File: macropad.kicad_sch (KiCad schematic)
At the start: 65 parts, among them J1 USB_C_Receptacle_USB2.0, J3 Conn_01x03, J6 Conn_01x04_Pin, J7 Conn_01x02_Pin, SW1 SW_Push, SW2 SW_Push, SW3 SW_Push, SW4 SW_Push, SW5 SW_Push, SW6 RotaryEncoder_Switch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

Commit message: Cleanup libraries
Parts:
- LED1, LED2, LED3, LED4, LED5, LED6: symbol marbastlib:SK6812MINI-E -> Marbastlib:SK6812MINI-E
- U3: symbol mcp5323:MIC5323-3.3YD5-TR -> Mcp5323:MIC5323-3.3YD5-TR
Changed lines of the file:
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@@
     )
   )
-  (symbol (lib_id "marbastlib:SK6812MINI-E") (at 228.6 118.11 0) (unit 1)
+  (symbol (lib_id "Marbastlib:SK6812MINI-E") (at 228.6 118.11 0) (unit 1)
     (in_bom yes) (on_board yes) (dnp no)
     (property "Reference" "LED4" (at 234.95 125.73 0)
@@
     )
   )
-  (symbol (lib_id "marbastlib:SK6812MINI-E") (at 193.04 118.11 0) (unit 1)
+  (symbol (lib_id "Marbastlib:SK6812MINI-E") (at 193.04 118.11 0) (unit 1)
     (in_bom yes) (on_board yes) (dnp no)
     (property "Reference" "LED2" (at 199.39 125.73 0)
@@
     )
   )
-  (symbol (lib_id "marbastlib:SK6812MINI-E") (at 175.26 118.11 0) (unit 1)
+  (symbol (lib_id "Marbastlib:SK6812MINI-E") (at 175.26 118.11 0) (unit 1)
     (in_bom yes) (on_board yes) (dnp no)
     (property "Reference" "LED1" (at 181.61 125.73 0)
@@
     )
   )
-  (symbol (lib_id "marbastlib:SK6812MINI-E") (at 246.38 118.11 0) (unit 1)
+  (symbol (lib_id "Marbastlib:SK6812MINI-E") (at 246.38 118.11 0) (unit 1)
     (in_bom yes) (on_board yes) (dnp no)
     (property "Reference" "LED5" (at 252.73 125.73 0)
@@
     )
   )
-  (symbol (lib_id "marbastlib:SK6812MINI-E") (at 264.16 118.11 0) (unit 1)
+  (symbol (lib_id "Marbastlib:SK6812MINI-E") (at 264.16 118.11 0) (unit 1)
     (in_bom yes) (on_board yes) (dnp no)
     (property "Reference" "LED6" (at 270.51 125.73 0)
@@
     )
   )
-  (symbol (lib_id "mcp5323:MIC5323-3.3YD5-TR") (at 35.56 168.91 0) (unit 1)
+  (symbol (lib_id "Mcp5323:MIC5323-3.3YD5-TR") (at 35.56 168.91 0) (unit 1)
     (in_bom yes) (on_board yes) (dnp no) (fields_autoplaced)
     (property "Reference" "U3" (at 49.53 161.29 0)
@@
     )
   )
-  (symbol (lib_id "marbastlib:SK6812MINI-E") (at 210.82 118.11 0) (unit 1)
+  (symbol (lib_id "Marbastlib:SK6812MINI-E") (at 210.82 118.11 0) (unit 1)
     (in_bom yes) (on_board yes) (dnp no)
     (property "Reference" "LED3" (at 217.17 125.73 0)

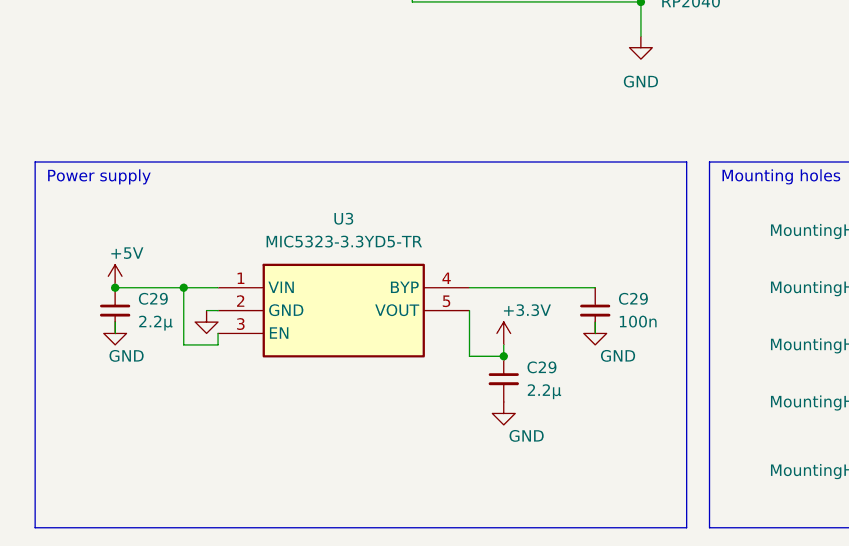
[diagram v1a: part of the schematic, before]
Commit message: Switch LDO for a cheaper part.
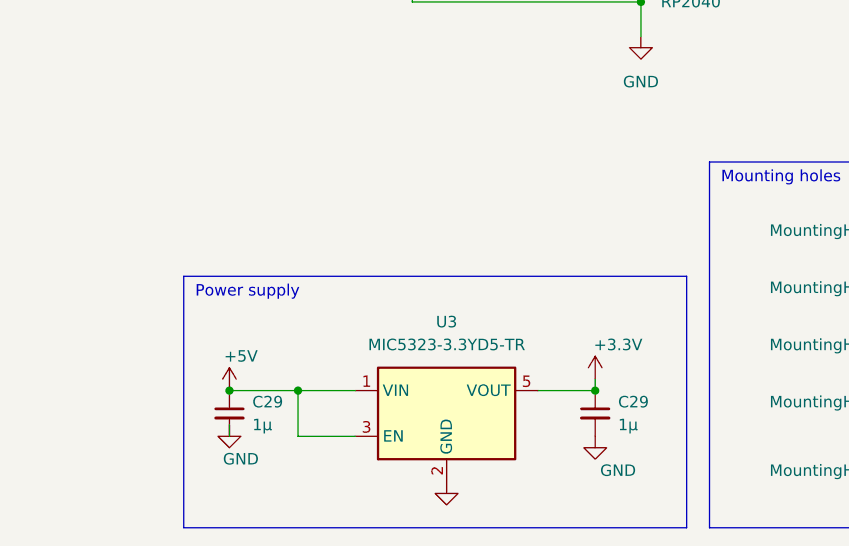
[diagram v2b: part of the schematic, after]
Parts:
- removed C29: 100n, Capacitor_SMD:C_0402_1005Metric, symbol Device:C_Small
- C29: value 2.2µ -> 1µ
- SW1: LCSC (none) -> C5333465
- U3: footprint Trackpad:SOT95P280X100-5N -> Package_TO_SOT_SMD:SOT-23-5; symbol Mcp5323:MIC5323-3.3YD5-TR -> Regulator_Linear:MIC5504-3.3YM5; LCSC C512211 -> C88419
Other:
- moved on the sheet: C29

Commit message: Move USB port closer to the edge, Additional silkscreen, Add reset header, shrink LDO caps, swap QSPI flash.
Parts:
- added J9: Conn_01x02_Pin, Connector_PinHeader_2.54mm:PinHeader_1x02_P2.54mm_Vertical, symbol Connector:Conn_01x02_Pin
- C29: footprint Capacitor_SMD:C_0603_1608Metric -> Capacitor_SMD:C_0402_1005Metric
- SW1: LCSC C5333465 -> (none)
- U2: value GD25Q80CEIGR -> W25Q16JVUXIQ
- U3: LCSC C88419 -> C512211
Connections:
- net D+: now also J1.A6 (D+), J1.B6 (D+), U7.1 (I/O1)
- net D-: now also J1.A7 (D-), J1.B7 (D-), U7.6 (I/O1)
- net GND: now also J9.2 (Pin_2)
- net RUN: now reaches U1.26 (RUN)
- net RUN: now also J9.1 (Pin_1)
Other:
- note added: "Reset Header"
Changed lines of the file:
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@@
   (junction (at 105.41 22.86) (diameter 0) (color 0 0 0 0)
   )
-  (junction (at 218.44 63.5) (diameter 0) (color 0 0 0 0)
-  )
   (junction (at 156.21 31.75) (diameter 0) (color 0 0 0 0)
   )
@@
   (junction (at 77.47 20.32) (diameter 0) (color 0 0 0 0)
   )
+  (junction (at 218.44 63.5) (diameter 0) (color 0 0 0 0)
+  )
   (junction (at 246.38 44.45) (diameter 0) (color 0 0 0 0)
   )
@@
   (junction (at 77.47 180.34) (diameter 0) (color 0 0 0 0)
   )
-  (junction (at 218.44 58.42) (diameter 0) (color 0 0 0 0)
-  )
   (junction (at 82.55 137.16) (diameter 0) (color 0 0 0 0)
   )
@@
   (junction (at 58.42 29.21) (diameter 0) (color 0 0 0 0)
   )
+  (junction (at 218.44 58.42) (diameter 0) (color 0 0 0 0)
+  )
   (junction (at 120.65 62.23) (diameter 0) (color 0 0 0 0)
   )
@@
     (stroke (width 0) (type default))
   )
-  (wire (pts (xy 218.44 63.5) (xy 247.65 63.5))
-    (stroke (width 0) (type default))
-  )
   (wire (pts (xy 175.26 100.33) (xy 179.07 100.33))
     (stroke (width 0) (type default))
@@
     (stroke (width 0) (type default))
   )
-  (wire (pts (xy 218.44 62.23) (xy 218.44 63.5))
+  (wire (pts (xy 222.25 63.5) (xy 218.44 63.5))
     (stroke (width 0) (type default))
   )
@@
     (stroke (width 0) (type default))
   )
-  (wire (pts (xy 218.44 63.5) (xy 218.44 64.77))
+  (wire (pts (xy 218.44 62.23) (xy 218.44 63.5))
     (stroke (width 0) (type default))
   )
@@
     (stroke (width 0) (type default))
   )
+  (wire (pts (xy 218.44 58.42) (xy 218.44 59.69))
+    (stroke (width 0) (type default))
+  )
   (wire (pts (xy 254 118.11) (xy 256.54 118.11))
     (stroke (width 0) (type default))
@@
     (stroke (width 0) (type default))
   )
+  (wire (pts (xy 222.25 58.42) (xy 218.44 58.42))
+    (stroke (width 0) (type default))
+  )
   (wire (pts (xy 210.82 100.33) (xy 210.82 110.49))
     (stroke (width 0) (type default))
@@
     (stroke (width 0) (type default))
   )
+  (wire (pts (xy 243.84 58.42) (xy 247.65 58.42))
+    (stroke (width 0) (type default))
+  )
   (wire (pts (xy 271.78 58.42) (xy 267.97 58.42))
     (stroke (width 0) (type default))
@@
     (stroke (width 0) (type default))
   )
+  (wire (pts (xy 243.84 63.5) (xy 247.65 63.5))
+    (stroke (width 0) (type default))
+  )
   (wire (pts (xy 124.46 64.77) (xy 130.81 64.77))
     (stroke (width 0) (type default))
@@
     (stroke (width 0) (type default))
   )
-  (wire (pts (xy 218.44 57.15) (xy 218.44 58.42))
-    (stroke (width 0) (type default))
-  )
   (wire (pts (xy 77.47 39.37) (xy 77.47 44.45))
     (stroke (width 0) (type default))
@@
     (stroke (width 0) (type default))
   )
+  (wire (pts (xy 80.01 156.21) (xy 76.2 156.21))
+    (stroke (width 0) (type default))
+  )
   (wire (pts (xy 58.42 29.21) (xy 68.58 29.21))
     (stroke (width 0) (type default))
@@
     (stroke (width 0) (type default))
   )
+  (wire (pts (xy 218.44 63.5) (xy 218.44 64.77))
+    (stroke (width 0) (type default))
+  )
   (wire (pts (xy 228.6 100.33) (xy 232.41 100.33))
     (stroke (width 0) (type default))
@@
     (stroke (width 0) (type default))
   )
-  (wire (pts (xy 218.44 58.42) (xy 247.65 58.42))
-    (stroke (width 0) (type default))
-  )
   (wire (pts (xy 120.65 62.23) (xy 130.81 62.23))
     (stroke (width 0) (type default))
@@
     (stroke (width 0) (type default))
   )
-  (wire (pts (xy 218.44 58.42) (xy 218.44 59.69))
+  (wire (pts (xy 218.44 57.15) (xy 218.44 58.42))
     (stroke (width 0) (type default))
   )
@@
     (fill (type none))
   )
+  (rectangle (start 57.15 149.86) (end 87.63 165.1)
+    (stroke (width 0) (type default))
+    (fill (type none))
+  )
   (rectangle (start 189.23 33.02) (end 280.67 88.9)
     (stroke (width 0) (type default))
@@
     (effects (font (size 1.27 1.27)) (justify left bottom))
   )
+  (text "Reset Header" (at 58.42 152.4 0)
+    (effects (font (size 1.27 1.27)) (justify left bottom))
+  )
   (text "5V LED\nData" (at 158.75 123.19 0)
     (effects (font (size 1.27 1.27)) (justify left bottom))
@@
     (effects (font (size 1.27 1.27)) (justify right bottom))
   )
+  (label "RUN" (at 80.01 156.21 0) (fields_autoplaced)
+    (effects (font (size 1.27 1.27)) (justify left bottom))
+  )
   (label "ENC2_A" (at 107.95 97.79 0) (fields_autoplaced)
     (effects (font (size 1.27 1.27)) (justify left bottom))
@@
     (effects (font (size 1.27 1.27)) (justify right bottom))
   )
+  (label "RUN" (at 57.15 52.07 180) (fields_autoplaced)
+    (effects (font (size 1.27 1.27)) (justify right bottom))
+  )
   (label "SW1" (at 151.13 147.32 0) (fields_autoplaced)
     (effects (font (size 1.27 1.27)) (justify left bottom))
@@
     (effects (font (size 1.27 1.27)) (justify left bottom))
   )
+  (label "D-" (at 243.84 58.42 180) (fields_autoplaced)
+    (effects (font (size 1.27 1.27)) (justify right bottom))
+  )
+  (label "D-" (at 222.25 58.42 0) (fields_autoplaced)
+    (effects (font (size 1.27 1.27)) (justify left bottom))
+  )
   (label "SW7" (at 234.95 152.4 180) (fields_autoplaced)
     (effects (font (size 1.27 1.27)) (justify right bottom))
@@
     (effects (font (size 1.27 1.27)) (justify right bottom))
   )
+  (label "D+" (at 222.25 63.5 0) (fields_autoplaced)
+    (effects (font (size 1.27 1.27)) (justify left bottom))
+  )
+  (label "D+" (at 243.84 63.5 180) (fields_autoplaced)
+    (effects (font (size 1.27 1.27)) (justify right bottom))
+  )
   (label "D-" (at 271.78 58.42 0) (fields_autoplaced)
     (effects (font (size 1.27 1.27)) (justify left bottom))
@@
       (effects (font (size 1.27 1.27)) (justify left))
     )
-    (property "Footprint" "Capacitor_SMD:C_0603_1608Metric" (at 77.47 182.88 0)
+    (property "Footprint" "Capacitor_SMD:C_0402_1005Metric" (at 77.47 182.88 0)
       (effects (font (size 1.27 1.27)) hide)
     )
@@
     )
   )
+  (symbol (lib_id "power:GND") (at 76.2 158.75 90) (unit 1)
+    (in_bom yes) (on_board yes) (dnp no) (fields_autoplaced)
+    (property "Reference" "#PWR01" (at 82.55 158.75 0)
+      (effects (font (size 1.27 1.27)) hide)
+    )
+    (property "Value" "GND" (at 80.01 158.75 90)
+      (effects (font (size 1.27 1.27)) (justify right))
+    )
+    (property "Footprint" "" (at 76.2 158.75 0)
+      (effects (font (size 1.27 1.27)) hide)
+    )
+    (property "Datasheet" "" (at 76.2 158.75 0)
+      (effects (font (size 1.27 1.27)) hide)
+    )
+    (pin "1")
+    (instances
+      (project "trackpad"
+        (path "/3796446b-0052-4d89-b512-07a2e9135d0d"
+          (reference "#PWR01") (unit 1)
+        )
+        (path "/3796446b-0052-4d89-b512-07a2e9135d0d/efc97fde-28db-4fd6-89b1-84dafa779b4e"
+          (reference "#PWR051") (unit 1)
+        )
+      )
+    )
+  )
   (symbol (lib_id "power:GND") (at 199.39 83.82 0) (unit 1)
     (in_bom yes) (on_board yes) (dnp no)
@@
       (effects (font (size 1.27 1.27)) (justify left))
     )
-    (property "Value" "GD25Q80CEIGR" (at 40.64 90.17 0)
+    (property "Value" "W25Q16JVUXIQ" (at 40.64 90.17 0)
       (effects (font (size 1.27 1.27)) (justify left))
     )
@@
       (effects (font (size 1.27 1.27)) (justify left))
     )
-    (property "Footprint" "Capacitor_SMD:C_0603_1608Metric" (at 36.83 182.88 0)
+    (property "Footprint" "Capacitor_SMD:C_0402_1005Metric" (at 36.83 182.88 0)
       (effects (font (size 1.27 1.27)) hide)
     )
@@
     )
   )
+  (symbol (lib_id "Connector:Conn_01x02_Pin") (at 71.12 156.21 0) (unit 1)
+    (in_bom yes) (on_board yes) (dnp no)
+    (property "Reference" "J9" (at 77.47 153.67 0)
+      (effects (font (size 1.27 1.27)))
+    )
+    (property "Value" "Conn_01x02_Pin" (at 68.58 161.29 0)
+      (effects (font (size 1.27 1.27)))
+    )
+    (property "Footprint" "Connector_PinHeader_2.54mm:PinHeader_1x02_P2.54mm_Vertical" (at 71.12 156.21 0)
+      (effects (font (size 1.27 1.27)) hide)
+    )
+    (property "Datasheet" "~" (at 71.12 156.21 0)
+      (effects (font (size 1.27 1.27)) hide)
+    )
+    (pin "1")
+    (pin "2")
+    (instances
+      (project "trackpad"
+        (path "/3796446b-0052-4d89-b512-07a2e9135d0d/efc97fde-28db-4fd6-89b1-84dafa779b4e"
+          (reference "J9") (unit 1)
+        )
+      )
+    )
+  )
   (symbol (lib_id "Device:D_Schottky") (at 242.57 44.45 0) (mirror y) (unit 1)
     (in_bom yes) (on_board yes) (dnp no)
@@
       (effects (font (size 1.27 1.27)) (justify left top) hide)
     )
-    (property "LCSC" "C88419" (at 74.93 175.26 0)
+    (property "LCSC" "C512211" (at 74.93 175.26 0)
       (effects (font (size 1.27 1.27)) hide)
     )
@@
       (effects (font (size 1.27 1.27)) hide)
     )
-    (property "LCSC" "C5333465" (at 38.1 44.45 0)
-      (effects (font (size 1.27 1.27)) hide)
-    )

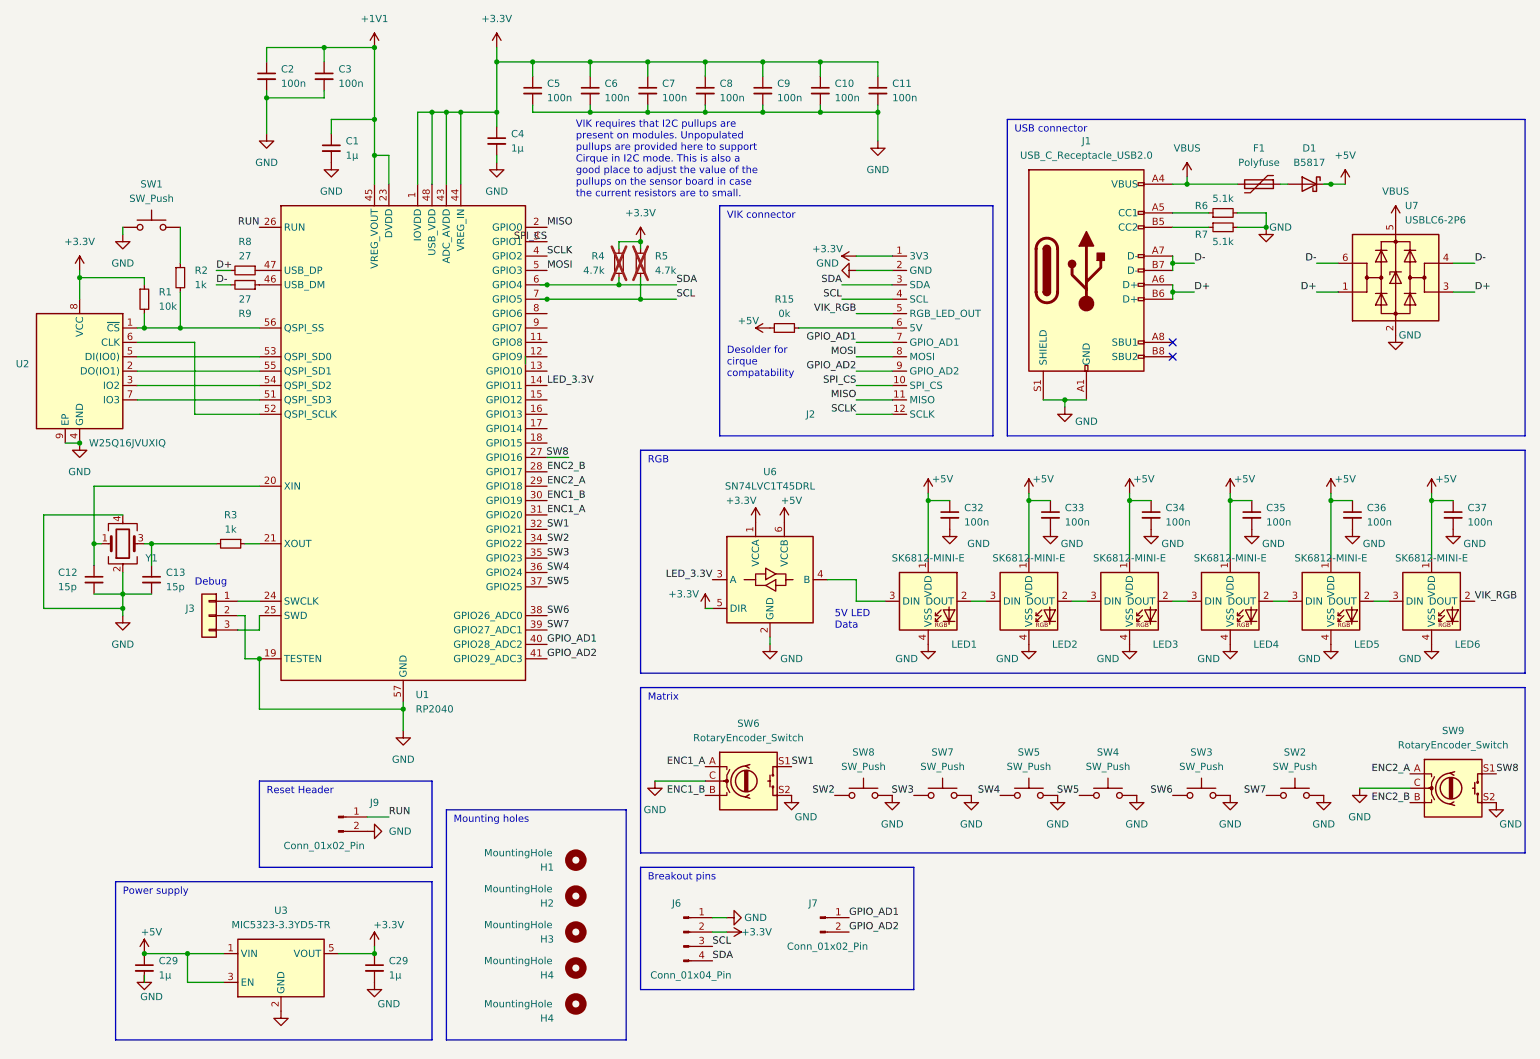
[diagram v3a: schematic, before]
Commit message: Re-route to avoid crossing the USB data lines. Reduced keys to 5 to avoid having to route a long trace around the crystal, swaped key footprint from choc hotswap to mx/choc combined soldered.
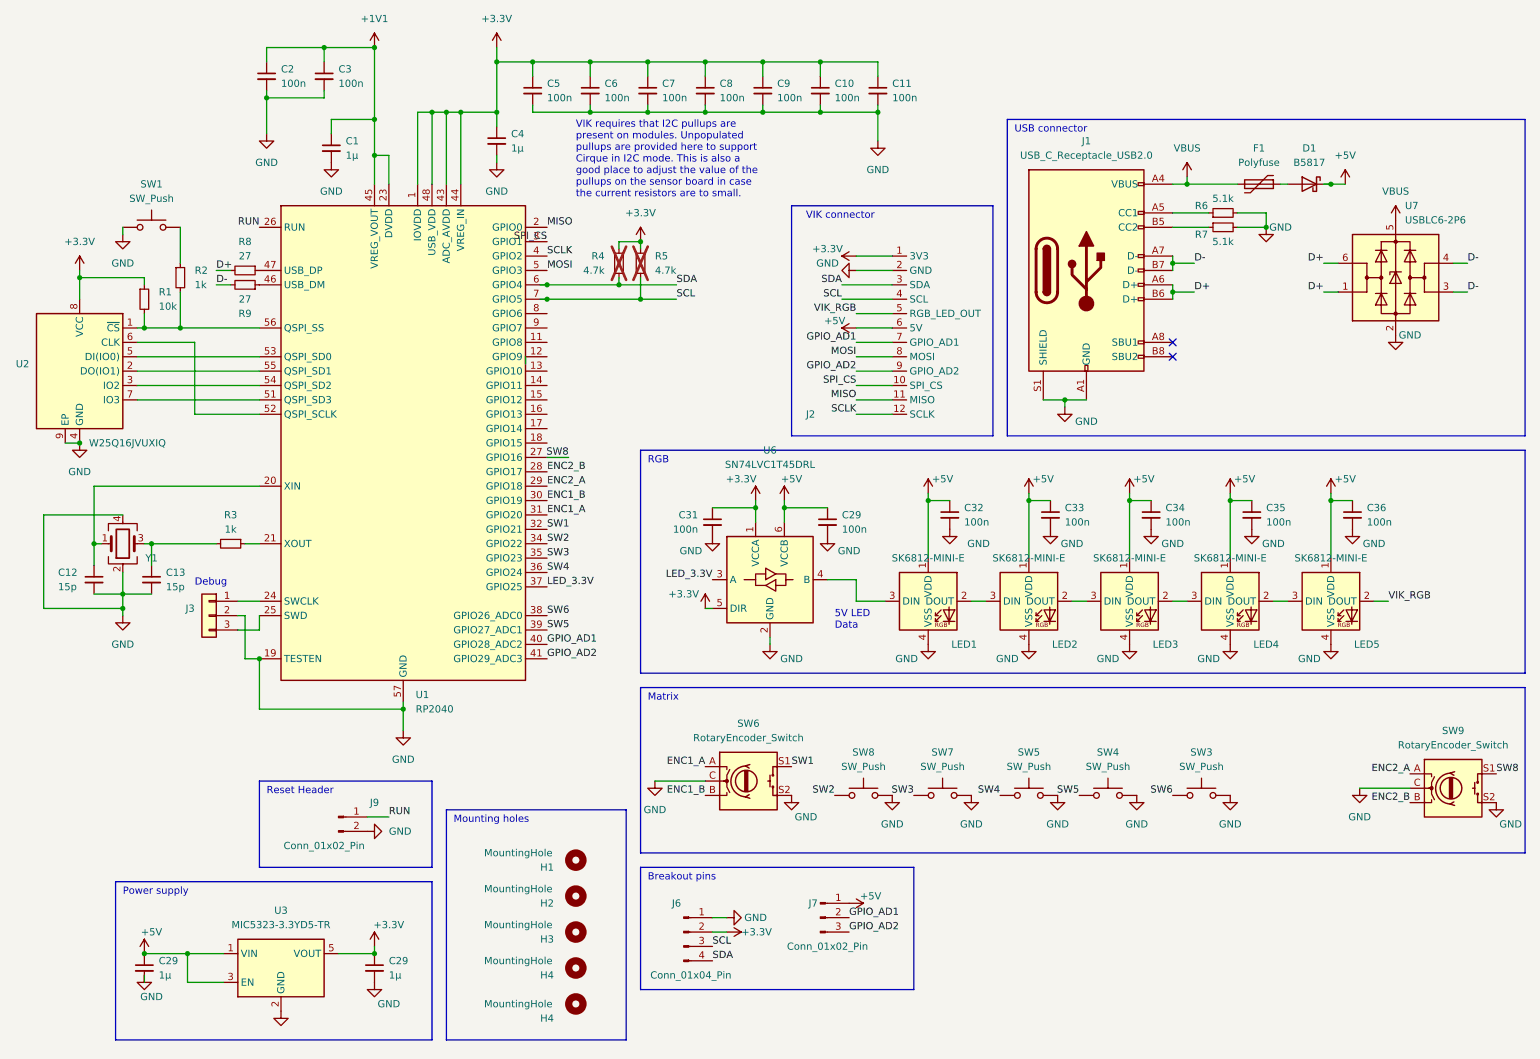
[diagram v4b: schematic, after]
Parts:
- removed C37: 100n, Capacitor_SMD:C_0402_1005Metric, symbol Device:C_Small
- removed LED6: SK6812-MINI-E, PCM_marbastlib-various:LED_6028R, symbol Marbastlib:SK6812MINI-E
- removed R15: 0k, Resistor_SMD:R_0402_1005Metric_Pad0.72x0.64mm_HandSolder, symbol Device:R_Small
- removed SW2: SW_Push, PCM_marbastlib-choc:SW_choc_v1_HS_1u, symbol Switch:SW_Push
- added C29, C31: 100n, Capacitor_SMD:C_0402_1005Metric, symbol Device:C_Small
- H2: footprint MountingHole:MountingHole_3.2mm_M3 -> MountingHole:MountingHole_2.2mm_M2
- J7: footprint Connector_PinHeader_2.54mm:PinHeader_1x02_P2.54mm_Vertical -> Connector_PinHeader_2.54mm:PinHeader_1x03_P2.54mm_Vertical; symbol Connector:Conn_01x02_Pin -> Connector:Conn_01x03_Pin
- SW3, SW4, SW5, SW7, SW8: footprint PCM_marbastlib-choc:SW_choc_v1_HS_1u -> PCM_marbastlib-xp-choc:SW_choc_MxCombo_1u
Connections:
- net SW7 is gone; now on net SW5: U1.39 (GPIO27_ADC1)
- net +3.3V: now also C31.1
- net +5V: now also J2.6 (5V), J7.1 (Pin_1), C29.1
- net D+: now also U7.6 (I/O1); no longer U7.3 (I/O2)
- net D-: now also U7.3 (I/O2); no longer U7.6 (I/O1)
- net GND: now also C29.2, C31.2
- net GPIO_AD1: now also J7.2 (Pin_2); no longer J7.1 (Pin_1)
- net GPIO_AD2: now also J7.3 (Pin_3); no longer J7.2 (Pin_2)
- net LED_3.3V: now also U1.37 (GPIO25); no longer U1.14 (GPIO11)
- net SW5: no longer U1.37 (GPIO25)
- net VIK_RGB: now also LED5.2 (DOUT)
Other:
- note removed: "Desolder for cirque compatability"
